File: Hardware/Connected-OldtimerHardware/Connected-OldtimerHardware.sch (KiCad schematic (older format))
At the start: 1 part, among them J1 Particle_Electron

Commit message: added modules
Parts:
- added J2: CAN_Tranceiver, symbol Connector_Generic:Conn_01x08
- added J3: FRAM, symbol Connector_Generic:Conn_01x08
- added J4: GPS_Module, symbol Connector_Generic:Conn_01x09
- added J5: CAN_Bus_Connector, symbol Connector_Generic:Conn_01x04
- added J6: Motion_Sensor, symbol Connector_Generic:Conn_01x03
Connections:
- net labels added: CAN_H, CAN_L
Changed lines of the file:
@@
 EESchema Schematic File Version 4
-EELAYER 26 0
+LIBS:Connected-OldtimerHardware-cache
+EELAYER 30 0
 EELAYER END
 $Descr A4 11693 8268
@@
 Text GLabel 3000 2050 2    50   Input ~ 0
 3V3
+$Comp
+L Connector_Generic:Conn_01x08 J2
+U 1 1 5D6706F9
+P 5450 2000
+F 0 "J2" H 5530 1992 50  0000 L CNN
+F 1 "CAN_Tranceiver" H 5530 1901 50  0000 L CNN
+F 2 "" H 5450 2000 50  0001 C CNN
+F 3 "~" H 5450 2000 50  0001 C CNN
+	1    5450 2000
+	1    0    0    -1
+$EndComp
+$Comp
+L Connector_Generic:Conn_01x08 J3
+U 1 1 5D6737BE
+P 5500 3450
+F 0 "J3" H 5580 3442 50  0000 L CNN
+F 1 "FRAM" H 5580 3351 50  0000 L CNN
+F 2 "" H 5500 3450 50  0001 C CNN
+F 3 "~" H 5500 3450 50  0001 C CNN
+	1    5500 3450
+	1    0    0    -1
+$EndComp
+$Comp
+L Connector_Generic:Conn_01x09 J4
+U 1 1 5D673A38
+P 5500 5100
+F 0 "J4" H 5580 5142 50  0000 L CNN
+F 1 "GPS_Module" H 5580 5051 50  0000 L CNN
+F 2 "" H 5500 5100 50  0001 C CNN
+F 3 "~" H 5500 5100 50  0001 C CNN
+	1    5500 5100
+	1    0    0    -1
+$EndComp
+Text GLabel 5250 1700 0    50   Input ~ 0
+VIN
+Text GLabel 5250 1800 0    50   Input ~ 0
+GND
+Text GLabel 5250 2100 0    50   Input ~ 0
+CAN_H
+Text GLabel 5250 2200 0    50   Input ~ 0
+CAN_L
+Text GLabel 5300 3150 0    50   Input ~ 0
+VIN
+Text GLabel 5300 3250 0    50   Input ~ 0
+GND
+Text GLabel 5300 3450 0    50   Input ~ 0
+D1
+Text GLabel 5300 3550 0    50   Input ~ 0
+D0
+Text GLabel 5300 5400 0    50   Input ~ 0
+VIN
+Text GLabel 5300 5300 0    50   Input ~ 0
+GND
+Text GLabel 5300 5200 0    50   Input ~ 0
+C1
+Text GLabel 5300 5100 0    50   Input ~ 0
+C0
+$Comp
+L Connector_Generic:Conn_01x04 J5
+U 1 1 5D676AB8
+P 7900 1750
+F 0 "J5" H 7980 1742 50  0000 L CNN
+F 1 "CAN_Bus_Connector" H 7980 1651 50  0000 L CNN
+F 2 "" H 7900 1750 50  0001 C CNN
+F 3 "~" H 7900 1750 50  0001 C CNN
+	1    7900 1750
+	1    0    0    -1
+$EndComp
+Text GLabel 7700 1650 0    50   Input ~ 0
+VIN
+Text GLabel 7700 1750 0    50   Input ~ 0
+GND
+Text GLabel 7700 1850 0    50   Input ~ 0
+CAN_H
+Text GLabel 7700 1950 0    50   Input ~ 0
+CAN_L
+$Comp
+L Connector_Generic:Conn_01x03 J6
+U 1 1 5D67913E
+P 7900 2750
+F 0 "J6" H 7980 2792 50  0000 L CNN
+F 1 "Motion_Sensor" H 7980 2701 50  0000 L CNN
+F 2 "" H 7900 2750 50  0001 C CNN
+F 3 "~" H 7900 2750 50  0001 C CNN
+	1    7900 2750
+	1    0    0    -1
+$EndComp
+Text GLabel 7700 2650 0    50   Input ~ 0
+3V3
+Text GLabel 7700 2750 0    50   Input ~ 0
+GND
+Text GLabel 7700 2850 0    50   Input ~ 0
+A0
 $EndSCHEMATC

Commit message: changed can bus to custom module
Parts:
- removed J2: CAN_Tranceiver, symbol Connector_Generic:Conn_01x08
- added U?: CANTranceiverModule, symbol HeathsComponents:CANTranceiverModule
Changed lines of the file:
@@
 EESchema Schematic File Version 4
 LIBS:Connected-OldtimerHardware-cache
-EELAYER 30 0
+EELAYER 26 0
 EELAYER END
 $Descr A4 11693 8268
@@
 3V3
 $Comp
-L Connector_Generic:Conn_01x08 J2
-U 1 1 5D6706F9
-P 5450 2000
-F 0 "J2" H 5530 1992 50  0000 L CNN
-F 1 "CAN_Tranceiver" H 5530 1901 50  0000 L CNN
-F 2 "" H 5450 2000 50  0001 C CNN
-F 3 "~" H 5450 2000 50  0001 C CNN
-	1    5450 2000
-	1    0    0    -1
-$EndComp
-$Comp
 L Connector_Generic:Conn_01x08 J3
 U 1 1 5D6737BE
@@
 	1    0    0    -1
 $EndComp
-Text GLabel 5250 1700 0    50   Input ~ 0
-VIN
-Text GLabel 5250 1800 0    50   Input ~ 0
-GND
-Text GLabel 5250 2100 0    50   Input ~ 0
-CAN_H
-Text GLabel 5250 2200 0    50   Input ~ 0
-CAN_L
 Text GLabel 5300 3150 0    50   Input ~ 0
 VIN
@@
 Text GLabel 7700 2850 0    50   Input ~ 0
 A0
+$Comp
+L HeathsComponents:CANTranceiverModule U?
+U 1 1 5D6CF6EA
+P 5800 1950
+F 0 "U?" H 5827 2096 50  0000 L CNN
+F 1 "CANTranceiverModule" H 5827 2005 50  0000 L CNN
+F 2 "" H 5800 1950 50  0001 C CNN
+F 3 "" H 5800 1950 50  0001 C CNN
+	1    5800 1950
+	1    0    0    -1
+$EndComp
 $EndSCHEMATC

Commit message: changed electron to module
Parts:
- removed J1: Particle_Electron, Particle:electron, symbol Connector_Generic:Conn_02x18_Counter_Clockwise
- added U?: ParticleElectron, symbol HeathsComponents:ParticleElectron
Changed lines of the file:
@@
 Comment4 ""
 $EndDescr
-$Comp
-L Connector_Generic:Conn_02x18_Counter_Clockwise J1
-U 1 1 5D662EEF
-P 2700 2850
-F 0 "J1" H 2750 3867 50  0000 C CNN
-F 1 "Particle_Electron" H 2750 3776 50  0000 C CNN
-F 2 "Particle:electron" H 2700 2850 50  0001 C CNN
-F 3 "~" H 2700 2850 50  0001 C CNN
-	1    2700 2850
-	1    0    0    -1
-$EndComp
-Text GLabel 2500 2050 0    50   Input ~ 0
+Text GLabel 2350 1700 0    50   Input ~ 0
 VIN
-Text GLabel 2500 2150 0    50   Input ~ 0
+Text GLabel 2350 1800 0    50   Input ~ 0
 GND
-Text GLabel 2500 2250 0    50   Input ~ 0
+Text GLabel 2350 1900 0    50   Input ~ 0
 TX
-Text GLabel 2500 2350 0    50   Input ~ 0
+Text GLabel 2350 2000 0    50   Input ~ 0
 RX
-Text GLabel 2500 2450 0    50   Input ~ 0
+Text GLabel 2350 2100 0    50   Input ~ 0
 WKP
-Text GLabel 2500 2550 0    50   Input ~ 0
+Text GLabel 2350 2200 0    50   Input ~ 0
 DAC
-Text GLabel 2500 2650 0    50   Input ~ 0
+Text GLabel 2350 2300 0    50   Input ~ 0
 A5
-Text GLabel 2500 2750 0    50   Input ~ 0
+Text GLabel 2350 2400 0    50   Input ~ 0
 A4
-Text GLabel 2500 2850 0    50   Input ~ 0
+Text GLabel 2350 2500 0    50   Input ~ 0
 A3
-Text GLabel 2500 2950 0    50   Input ~ 0
+Text GLabel 2350 2600 0    50   Input ~ 0
 A2
-Text GLabel 2500 3050 0    50   Input ~ 0
+Text GLabel 2350 2700 0    50   Input ~ 0
 A1
-Text GLabel 2500 3150 0    50   Input ~ 0
+Text GLabel 2350 2800 0    50   Input ~ 0
 A0
-Text GLabel 2500 3250 0    50   Input ~ 0
+Text GLabel 2350 2900 0    50   Input ~ 0
 B5
-Text GLabel 2500 3350 0    50   Input ~ 0
+Text GLabel 2350 3000 0    50   Input ~ 0
 B4
-Text GLabel 2500 3450 0    50   Input ~ 0
+Text GLabel 2350 3100 0    50   Input ~ 0
 B3
-Text GLabel 2500 3550 0    50   Input ~ 0
+Text GLabel 2350 3200 0    50   Input ~ 0
 B2
-Text GLabel 2500 3650 0    50   Input ~ 0
+Text GLabel 2350 3300 0    50   Input ~ 0
 B1
-Text GLabel 2500 3750 0    50   Input ~ 0
+Text GLabel 2350 3400 0    50   Input ~ 0
 B0
-Text GLabel 3000 3750 2    50   Input ~ 0
-C0
-Text GLabel 3000 3650 2    50   Input ~ 0
-C1
-Text GLabel 3000 3550 2    50   Input ~ 0
-C2
-Text GLabel 3000 3450 2    50   Input ~ 0
-C3
-Text GLabel 3000 3350 2    50   Input ~ 0
-C4
-Text GLabel 3000 3250 2    50   Input ~ 0
-C5
-Text GLabel 3000 3150 2    50   Input ~ 0
-D0
-Text GLabel 3000 3050 2    50   Input ~ 0
-D1
-Text GLabel 3000 2950 2    50   Input ~ 0
-D2
-Text GLabel 3000 2850 2    50   Input ~ 0
-D3
-Text GLabel 3000 2750 2    50   Input ~ 0
-D4
-Text GLabel 3000 2650 2    50   Input ~ 0
-D5
-Text GLabel 3000 2550 2    50   Input ~ 0
-D6
-Text GLabel 3000 2450 2    50   Input ~ 0
-D7
-Text GLabel 3000 2350 2    50   Input ~ 0
-GND
-Text GLabel 3000 2250 2    50   Input ~ 0
-VBAT
-Text GLabel 3000 2150 2    50   Input ~ 0
-RESET
-Text GLabel 3000 2050 2    50   Input ~ 0
-3V3
 $Comp
 L Connector_Generic:Conn_01x08 J3
@@
 	1    0    0    -1
 $EndComp
+$Comp
+L HeathsComponents:ParticleElectron U?
+U 1 1 5D6D05D3
+P 3100 2300
+F 0 "U?" H 3075 3165 50  0000 C CNN
+F 1 "ParticleElectron" H 3075 3074 50  0000 C CNN
+F 2 "" H 3100 2300 50  0001 C CNN
+F 3 "" H 3100 2300 50  0001 C CNN
+	1    3100 2300
+	1    0    0    -1
+$EndComp
+Text GLabel 3800 1700 2    50   Input ~ 0
+3V3
+Text GLabel 3800 1800 2    50   Input ~ 0
+RESET
+Text GLabel 3800 1900 2    50   Input ~ 0
+VBAT
+Text GLabel 3800 2000 2    50   Input ~ 0
+GND
+Text GLabel 3800 2100 2    50   Input ~ 0
+D7
+Text GLabel 3800 2200 2    50   Input ~ 0
+D6
+Text GLabel 3800 2300 2    50   Input ~ 0
+D5
+Text GLabel 3800 2400 2    50   Input ~ 0
+D4
+Text GLabel 3800 2500 2    50   Input ~ 0
+D3
+Text GLabel 3800 2600 2    50   Input ~ 0
+D2
+Text GLabel 3800 2700 2    50   Input ~ 0
+D1
+Text GLabel 3800 2800 2    50   Input ~ 0
+D0
+Text GLabel 3800 2900 2    50   Input ~ 0
+C5
+Text GLabel 3800 3000 2    50   Input ~ 0
+C4
+Text GLabel 3800 3100 2    50   Input ~ 0
+C3
+Text GLabel 3800 3200 2    50   Input ~ 0
+C2
+Text GLabel 3800 3300 2    50   Input ~ 0
+C1
+Text GLabel 3800 3400 2    50   Input ~ 0
+C0
 $EndSCHEMATC

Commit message: rest of module conversions
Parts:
- removed J3: FRAM, symbol Connector_Generic:Conn_01x08
- removed J4: GPS_Module, symbol Connector_Generic:Conn_01x09
- removed J6: Motion_Sensor, symbol Connector_Generic:Conn_01x03
- added U?: AdafruitFRAM, symbol HeathsComponents:AdafruitFRAM
- added U?: AdafruitUltimateGPS, symbol HeathsComponents:AdafruitUltimateGPS
- added U?: MotionSensor, symbol HeathsComponents:MotionSensor
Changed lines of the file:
@@
 Text GLabel 2350 3400 0    50   Input ~ 0
 B0
-$Comp
-L Connector_Generic:Conn_01x08 J3
-U 1 1 5D6737BE
-P 5500 3450
-F 0 "J3" H 5580 3442 50  0000 L CNN
-F 1 "FRAM" H 5580 3351 50  0000 L CNN
-F 2 "" H 5500 3450 50  0001 C CNN
-F 3 "~" H 5500 3450 50  0001 C CNN
-	1    5500 3450
-	1    0    0    -1
-$EndComp
-$Comp
-L Connector_Generic:Conn_01x09 J4
-U 1 1 5D673A38
-P 5500 5100
-F 0 "J4" H 5580 5142 50  0000 L CNN
-F 1 "GPS_Module" H 5580 5051 50  0000 L CNN
-F 2 "" H 5500 5100 50  0001 C CNN
-F 3 "~" H 5500 5100 50  0001 C CNN
-	1    5500 5100
-	1    0    0    -1
-$EndComp
-Text GLabel 5300 3150 0    50   Input ~ 0
+Text GLabel 5000 3200 0    50   Input ~ 0
 VIN
-Text GLabel 5300 3250 0    50   Input ~ 0
+Text GLabel 5000 3300 0    50   Input ~ 0
 GND
-Text GLabel 5300 3450 0    50   Input ~ 0
+Text GLabel 5000 3500 0    50   Input ~ 0
 D1
-Text GLabel 5300 3550 0    50   Input ~ 0
+Text GLabel 5000 3600 0    50   Input ~ 0
 D0
-Text GLabel 5300 5400 0    50   Input ~ 0
+Text GLabel 4950 5600 0    50   Input ~ 0
 VIN
-Text GLabel 5300 5300 0    50   Input ~ 0
+Text GLabel 4950 5500 0    50   Input ~ 0
 GND
-Text GLabel 5300 5200 0    50   Input ~ 0
+Text GLabel 4950 5400 0    50   Input ~ 0
 C1
-Text GLabel 5300 5100 0    50   Input ~ 0
+Text GLabel 4950 5300 0    50   Input ~ 0
 C0
 $Comp
@@
 Text GLabel 7700 1950 0    50   Input ~ 0
 CAN_L
-$Comp
-L Connector_Generic:Conn_01x03 J6
-U 1 1 5D67913E
-P 7900 2750
-F 0 "J6" H 7980 2792 50  0000 L CNN
-F 1 "Motion_Sensor" H 7980 2701 50  0000 L CNN
-F 2 "" H 7900 2750 50  0001 C CNN
-F 3 "~" H 7900 2750 50  0001 C CNN
-	1    7900 2750
-	1    0    0    -1
-$EndComp
-Text GLabel 7700 2650 0    50   Input ~ 0
+Text GLabel 7800 3150 0    50   Input ~ 0
 3V3
-Text GLabel 7700 2750 0    50   Input ~ 0
+Text GLabel 7800 3250 0    50   Input ~ 0
 GND
-Text GLabel 7700 2850 0    50   Input ~ 0
+Text GLabel 7800 3350 0    50   Input ~ 0
 A0
 $Comp
@@
 Text GLabel 3800 3400 2    50   Input ~ 0
 C0
+$Comp
+L HeathsComponents:AdafruitFRAM U?
+U 1 1 5D6D08AC
+P 5450 3450
+F 0 "U?" H 5928 3396 50  0000 L CNN
+F 1 "AdafruitFRAM" H 5928 3305 50  0000 L CNN
+F 2 "" H 5450 3450 50  0001 C CNN
+F 3 "" H 5450 3450 50  0001 C CNN
+	1    5450 3450
+	1    0    0    -1
+$EndComp
+$Comp
+L HeathsComponents:AdafruitUltimateGPS U?
+U 1 1 5D6D0C95
+P 5600 5350
+F 0 "U?" H 5977 5421 50  0000 L CNN
+F 1 "AdafruitUltimateGPS" H 5977 5330 50  0000 L CNN
+F 2 "" H 5600 5350 50  0001 C CNN
+F 3 "" H 5600 5350 50  0001 C CNN
+	1    5600 5350
+	1    0    0    -1
+$EndComp
+$Comp
+L HeathsComponents:MotionSensor U?
+U 1 1 5D6D1163
+P 8200 3250
+F 0 "U?" H 8277 3296 50  0000 L CNN
+F 1 "MotionSensor" H 8277 3205 50  0000 L CNN
+F 2 "" H 8200 3250 50  0001 C CNN
+F 3 "" H 8200 3250 50  0001 C CNN
+	1    8200 3250
+	1    0    0    -1
+$EndComp
 $EndSCHEMATC

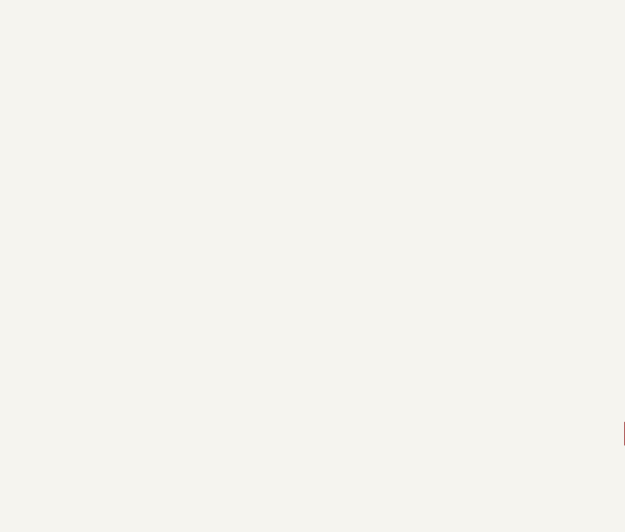
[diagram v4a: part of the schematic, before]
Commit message: added 12 to 5 V Switching Regulator
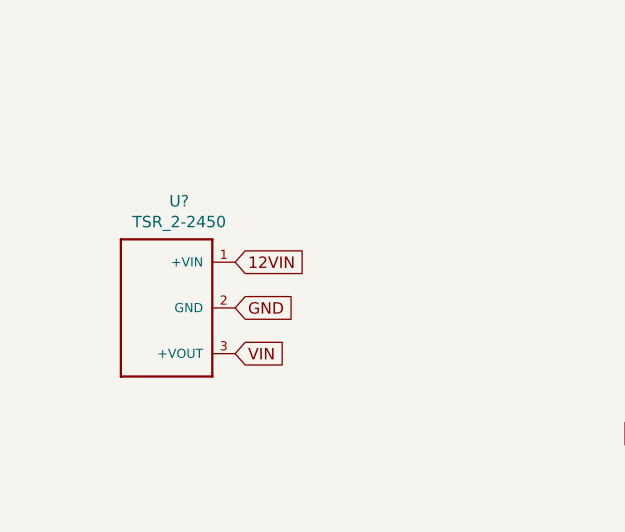
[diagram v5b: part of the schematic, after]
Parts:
- added U?: TSR_2-2450, SIP750W46P254L1400H1010Q3, symbol DCDC:TSR_2-2450
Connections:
- net GND: now also U?.2 (GND)
- net VIN: now also U?.3 (+VOUT)
- new net 12VIN: U?.1 (+VIN)
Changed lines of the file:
@@
 	1    0    0    -1
 $EndComp
+$Comp
+L DCDC:TSR_2-2450 U?
+U 1 1 5D6D21AF
+P 2700 4950
+F 0 "U?" H 2755 5417 50  0000 C CNN
+F 1 "TSR_2-2450" H 2755 5326 50  0000 C CNN
+F 2 "SIP750W46P254L1400H1010Q3" H 2700 4950 50  0001 L BNN
+F 3 "SIP-3 Tracopower" H 2700 4950 50  0001 L BNN
+F 4 "TSR 2-2450" H 2700 4950 50  0001 L BNN "Field4"
+F 5 "Unavailable" H 2700 4950 50  0001 L BNN "Field5"
+F 6 "Traco Power" H 2700 4950 50  0001 L BNN "Field6"
+F 7 "None" H 2700 4950 50  0001 L BNN "Field7"
+F 8 "DC-DC Point of Load _POL_ Converter PCB mount; Input 6.5-36Vdc; Output 5Vdc at 2A; SIP Through hole package" H 2700 4950 50  0001 L BNN "Field8"
+	1    2700 4950
+	1    0    0    -1
+$EndComp
+Text GLabel 3000 4750 2    50   Input ~ 0
+12VIN
+Text GLabel 3000 4950 2    50   Input ~ 0
+GND
+Text GLabel 3000 5150 2    50   Input ~ 0
+VIN
 $EndSCHEMATC
